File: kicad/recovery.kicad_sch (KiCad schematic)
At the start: 40 parts, among them J1 Bus_PCI_Express_x1, J4 Conn_01x02, J6 USB_C_Receptacle_USB2.0_16P, U2 RP2040, U4 W25Q128JVP, U9 MCP25625T-E/ML, X1 ABM8-272-T3, Y2 X322516MLB4SI

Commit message: update libraries
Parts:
- removed U9: MCP25625T-E/ML, MCP25625T_E_ML:QFN28_6X6MC_MCH, symbol MCP25625:MCP25625T-E_ML
- removed X1: ABM8-272-T3, ABM8-272-T3:ABM8-272-T3_ABR, symbol crystal:ABM8-272-T3
- removed Y2: X322516MLB4SI, X322516MLB4SI:OSC_X322516MLB4SI, symbol X322516MLB4SI:X322516MLB4SI
- added U1: MCP25625T-E/ML, 4in-kicad-library:QFN28_6X6MC_MCH, symbol 4in-kicad-library:MCP25625T-E_ML
- added X2: RP2040 Crystal, 4in-kicad-library:ABM8-272-T3_ABR, symbol 4in-kicad-library:ABM8-272-T3
- added Y1: X322516MLB4SI, 4in-kicad-library:X322516MLB4SI, symbol 4in-kicad-library:X322516MLB4SI
- C10, C11: LCSC PN (none) -> C1548
- C206, C207, C209, C211, C212, C213, C214, C215, C216, C40, C90, C92, C93: LCSC PN (none) -> C307331
- C208, C210: LCSC PN (none) -> C52923
- C94, C95: LCSC PN (none) -> C1555
- D1, D2: LCSC PN (none) -> C2286
- J1, J4: LCSC PN (none) -> n/a
- J6: LCSC PN (none) -> C2765186
- R1, R2: value 150 -> 1k; JLC Link https://jlcpcb.com/partdetail/23535-0603WAF1500T5E/C22808 -> https://jlcpcb.com/partdetail/12256-0402WGF1001TCE/C11702; LCSC PN (none) -> C11702; LCSC Part # C22808 -> C11702; price C$0.0013 -> C$0.0007
- R12, R30: LCSC PN (none) -> C11702
- R203, R204: LCSC PN (none) -> C25100
- R3, R4: LCSC PN (none) -> C25905
- R91: LCSC PN (none) -> C25744
- S1, S2: LCSC PN (none) -> C318884
- U2: LCSC C2040 -> (none); LCSC PN (none) -> C2040
- U4: footprint Package_SON:WSON-8-1EP_6x5mm_P1.27mm_EP3.4x4.3mm -> Package_SON:Fairchild_MicroPak-6_1.0x1.45mm_P0.5mm; LCSC C190862 -> (none); LCSC PN (none) -> C190862
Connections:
- net +3.3V: now also U1.11 (VIO), U1.3 (VDD)
- net +5V: now also U1.19 (VDDA)
- net CANINT: now also U1.25 (*INT)
- net CANN: now also U1.12 (CANL)
- net CANP: now also U1.13 (CANH)
- net CANRESET: now also U1.2 (*RESET)
- net CANSTBY: now also U1.15 (STBY)
- net CS: now also U1.1 (*CS)
- net GND: now also U1.18 (VSS), U1.22 (GND), U1.29 (EPAD), X2.2, X2.4, Y1.2, Y1.4
- net OSC1: now also U1.21 (OSC1), Y1.1
- net OSC2: now also U1.20 (OSC2), Y1.3
- net SCK: now also U1.26 (SCK)
- net SI: now also U1.27 (SI)
- net SO: now also U1.28 (SO)
- net XIN: now also X2.1
- net XOUT_pre: now also X2.3
- net rx: now also U1.10 (RXD), U1.5 (RXCAN)
- net tx: now also U1.16 (TXD), U1.4 (TXCAN)

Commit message: add wago connectors, update components with chips from new library
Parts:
- removed J4: Conn_01x02, Connector_PinHeader_2.54mm:PinHeader_1x02_P2.54mm_Vertical, symbol Connector_Generic:Conn_01x02
- removed S1, S2: TS-1187A-B-A-B, TS-1187A-B-A-B:SW_TS-1187A-B-A-B, symbol TS-1187A-B-A-B:TS-1187A-B-A-B
- added J2, J3: wago 2060-452/998-404, recovery:wago-2060-452_998-404, symbol recovery:wago-2060-452_998-404
- added J4: Conn_01x04, Connector:NS-Tech_Grove_1x04_P2mm_Vertical, symbol Connector_Generic:Conn_01x04
- added S1, S2: TS-1187A-B-A-B, 4in-kicad-library:TS-1187A-B-A-B, symbol 4in-kicad-library:TS-1187A-B-A-B
- U4: footprint Package_SON:Fairchild_MicroPak-6_1.0x1.45mm_P0.5mm -> Package_SON:WSON-8-1EP_6x5mm_P1.27mm_EP3.4x4.3mm
- renumbered U1 to U9, X2 to X1, Y1 to Y2
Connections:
- net +3.3V: now also J4.3 (Pin_3)
- net GND: now also J4.4 (Pin_4), S1.A, S1.B, S2.A, S2.B
- net RUN: now also S2.C, S2.D
- net SWCLK: now also J4.1 (Pin_1)
- net SWD: now also J4.2 (Pin_2)
- net ~{USB_BOOT_S}: now also S1.C, S1.D
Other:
- moved on the sheet: D2, R2

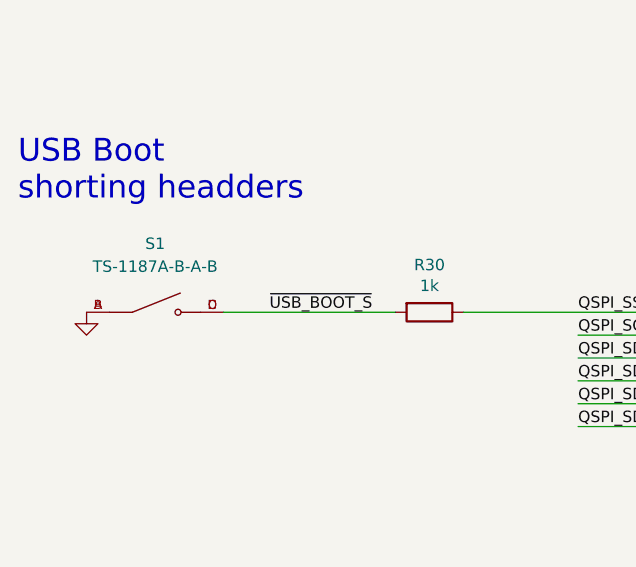
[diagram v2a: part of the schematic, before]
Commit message: rename symbol and footprint editor
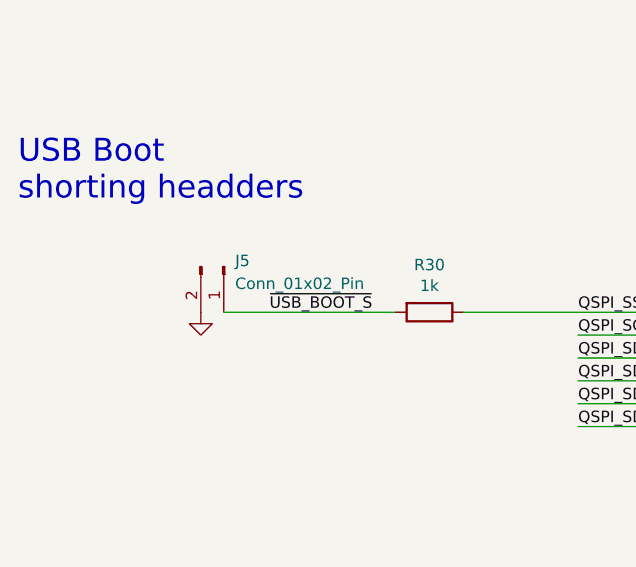
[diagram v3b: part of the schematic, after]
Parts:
- removed S1: TS-1187A-B-A-B, 4in-kicad-library:TS-1187A-B-A-B, symbol 4in-kicad-library:TS-1187A-B-A-B
- added J5: Conn_01x02_Pin, Connector_PinHeader_2.54mm:PinHeader_1x02_P2.54mm_Vertical, symbol Connector:Conn_01x02_Pin
- J4: footprint Connector:NS-Tech_Grove_1x04_P2mm_Vertical -> Connector_PinHeader_2.54mm:PinHeader_1x04_P2.54mm_Vertical
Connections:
- net GND: now also J5.2 (Pin_2)
- net ~{USB_BOOT_S}: now also J5.1 (Pin_1)
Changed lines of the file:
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@@
 	)
 	(symbol
+		(lib_id "Connector:Conn_01x02_Pin")
+		(at 69.85 162.56 270)
+		(unit 1)
+		(exclude_from_sim no)
+		(in_bom yes)
+		(on_board yes)
+		(dnp no)
+		(fields_autoplaced yes)
+		(property "Reference" "J5"
+			(at 71.12 161.9249 90)
+			(effects
+				(font
+					(size 1.27 1.27)
+				)
+				(justify left)
+			)
+		)
+		(property "Value" "Conn_01x02_Pin"
+			(at 71.12 164.4649 90)
+			(effects
+				(font
+					(size 1.27 1.27)
+				)
+				(justify left)
+			)
+		)
+		(property "Footprint" "Connector_PinHeader_2.54mm:PinHeader_1x02_P2.54mm_Vertical"
+			(at 69.85 162.56 0)
+			(effects
+				(font
+					(size 1.27 1.27)
+				)
+				(hide yes)
+			)
+		)
+		(property "Datasheet" "~"
+			(at 69.85 162.56 0)
+			(effects
+				(font
+					(size 1.27 1.27)
+				)
+				(hide yes)
+			)
+		)
+		(property "Description" "Generic connector, single row, 01x02, script generated"
+			(at 69.85 162.56 0)
+			(effects
+				(font
+					(size 1.27 1.27)
+				)
+				(hide yes)
+			)
+		)
+		(pin "1"
+		)
+		(pin "2"
+		)
+		(instances
+			(project ""
+				(path "/612ece3f-e722-4b33-8111-645d24cfcf05"
+					(reference "J5")
+					(unit 1)
+				)
+			)
+		)
+	)
+	(symbol
 		(lib_id "power:GND")
 		(at 274.32 219.71 0)
@@
 	(symbol
 		(lib_id "power:GND")
-		(at 54.61 167.64 0)
+		(at 67.31 167.64 0)
 		(unit 1)
 		(exclude_from_sim no)
@@
 		(dnp no)
 		(property "Reference" "#PWR011"
-			(at 54.61 173.99 0)
+			(at 67.31 173.99 0)
 			(effects
 				(font
@@
 		)
 		(property "Value" "GND"
-			(at 54.737 172.0342 0)
+			(at 67.437 172.0342 0)
 			(effects
 				(font
@@
 		)
 		(property "Footprint" ""
-			(at 54.61 167.64 0)
+			(at 67.31 167.64 0)
 			(effects
 				(font
@@
 		)
 		(property "Datasheet" ""
-			(at 54.61 167.64 0)
+			(at 67.31 167.64 0)
 			(effects
 				(font
@@
 		)
 		(property "Description" ""
-			(at 54.61 167.64 0)
+			(at 67.31 167.64 0)
 			(effects
 				(font
@@
 			)
 		)
-		(property "Footprint" "Connector:NS-Tech_Grove_1x04_P2mm_Vertical"
+		(property "Footprint" "Connector_PinHeader_2.54mm:PinHeader_1x04_P2.54mm_Vertical"
 			(at 243.84 212.09 0)
 			(effects
@@
 					(unit 1)
 				)
-			)
-		)
-	)
-	(symbol
-		(lib_id "4in-kicad-library:TS-1187A-B-A-B")
-		(at 62.23 167.64 0)
-		(unit 1)
-		(exclude_from_sim no)
-		(in_bom yes)
-		(on_board yes)
-		(dnp no)
-		(fields_autoplaced yes)
-		(property "Reference" "S1"
-			(at 62.23 160.02 0)
-			(effects
-				(font
-					(size 1.27 1.27)
-				)
-			)
-		)
-		(property "Value" "TS-1187A-B-A-B"
-			(at 62.23 162.56 0)
-			(effects
-				(font
-					(size 1.27 1.27)
-				)
-			)
-		)
-		(property "Footprint" "4in-kicad-library:TS-1187A-B-A-B"
-			(at 62.23 167.64 0)
-			(effects
-				(font
-					(size 1.27 1.27)
-				)
-				(justify bottom)
-				(hide yes)
-			)
-		)
-		(property "Datasheet" "https://jlcpcb.com/api/file/downloadByFileSystemAccessId/8550724022091735041"
-			(at 62.23 167.64 0)
-			(effects
-				(font
-					(size 1.27 1.27)
-				)
-				(hide yes)
-			)
-		)
-		(property "Description" "Button"
-			(at 62.23 167.64 0)
-			(effects
-				(font
-					(size 1.27 1.27)
-				)
-				(hide yes)
-			)
-		)
-		(property "JLC Link" "https://jlcpcb.com/partdetail/XKBConnection-TS_1187A_B_AB/C318884"
-			(at 62.23 167.64 0)
-			(effects
-				(font
-					(size 1.27 1.27)
-				)
-				(hide yes)
-			)
-		)
-		(property "LCSC PN" "C318884"
-			(at 62.23 167.64 0)
-			(effects
-				(font
-					(size 1.27 1.27)
-				)
-				(hide yes)
-			)
-		)
-		(property "JLC Price" "0.0242 "
-			(at 62.23 167.64 0)
-			(effects
-				(font
-					(size 1.27 1.27)
-				)
-				(hide yes)
-			)
-		)
-		(property "Manufacturer PN" "TS-1187A-B-A-B"
-			(at 62.23 167.64 0)
-			(effects
-				(font
-					(size 1.27 1.27)
-				)
-				(hide yes)
-			)
-		)
-		(pin "C"
-		)
-		(pin "D"
-		)
-		(pin "A"
-		)
-		(pin "B"
-		)
-		(instances
-			(project ""
-				(path "/612ece3f-e722-4b33-8111-645d24cfcf05"
-					(reference "S1")
-					(unit 1)
-				)

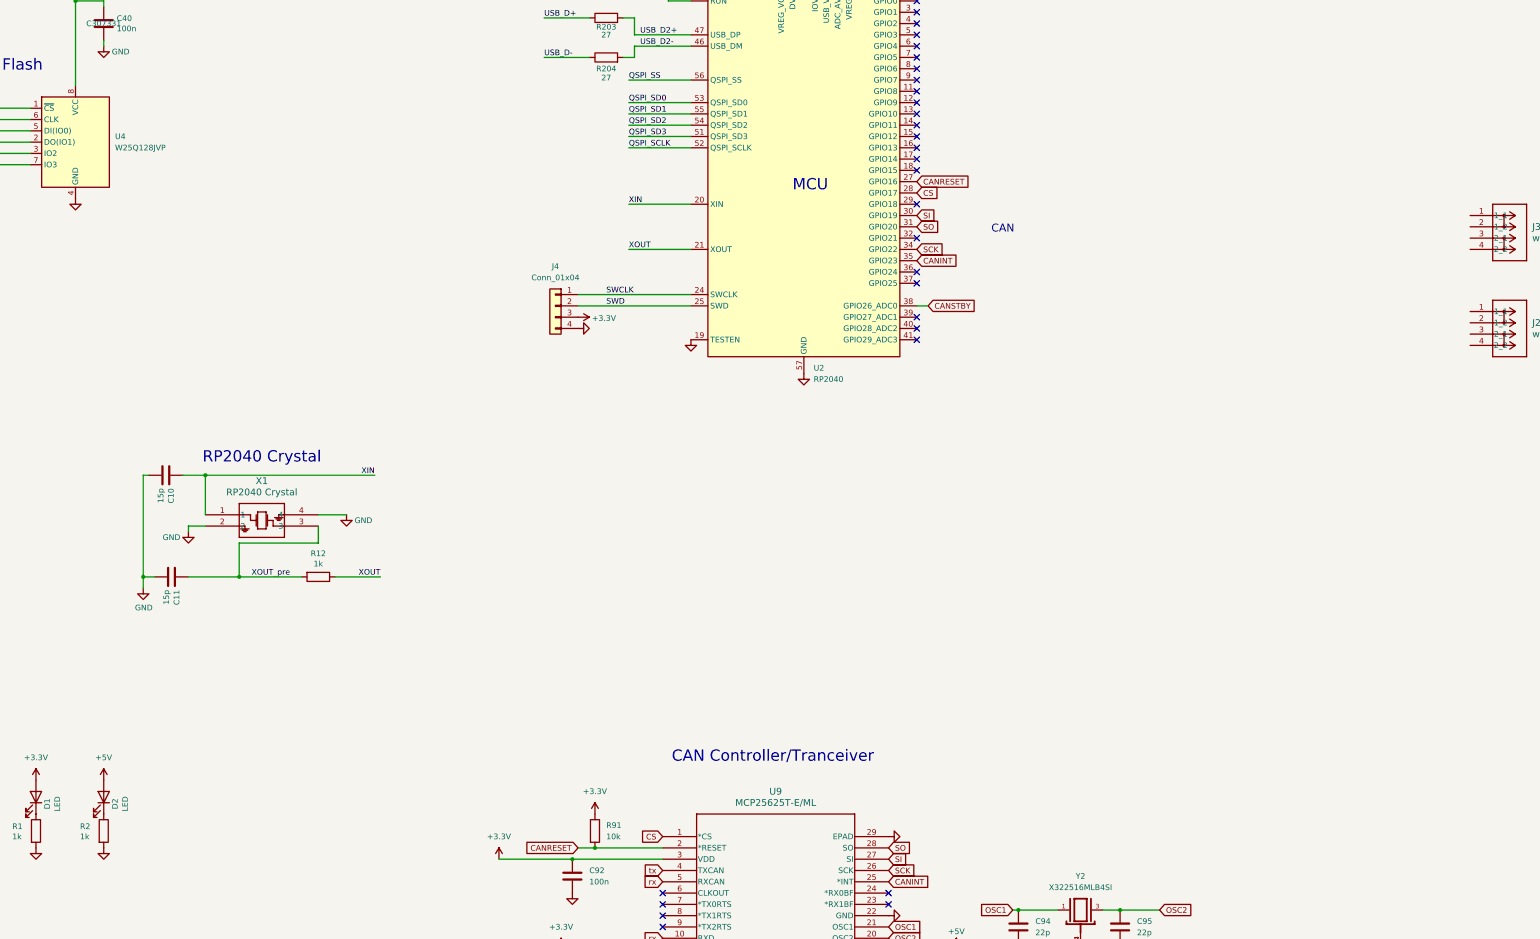
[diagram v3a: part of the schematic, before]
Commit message: add dual N channel mosfet symbol and footprint
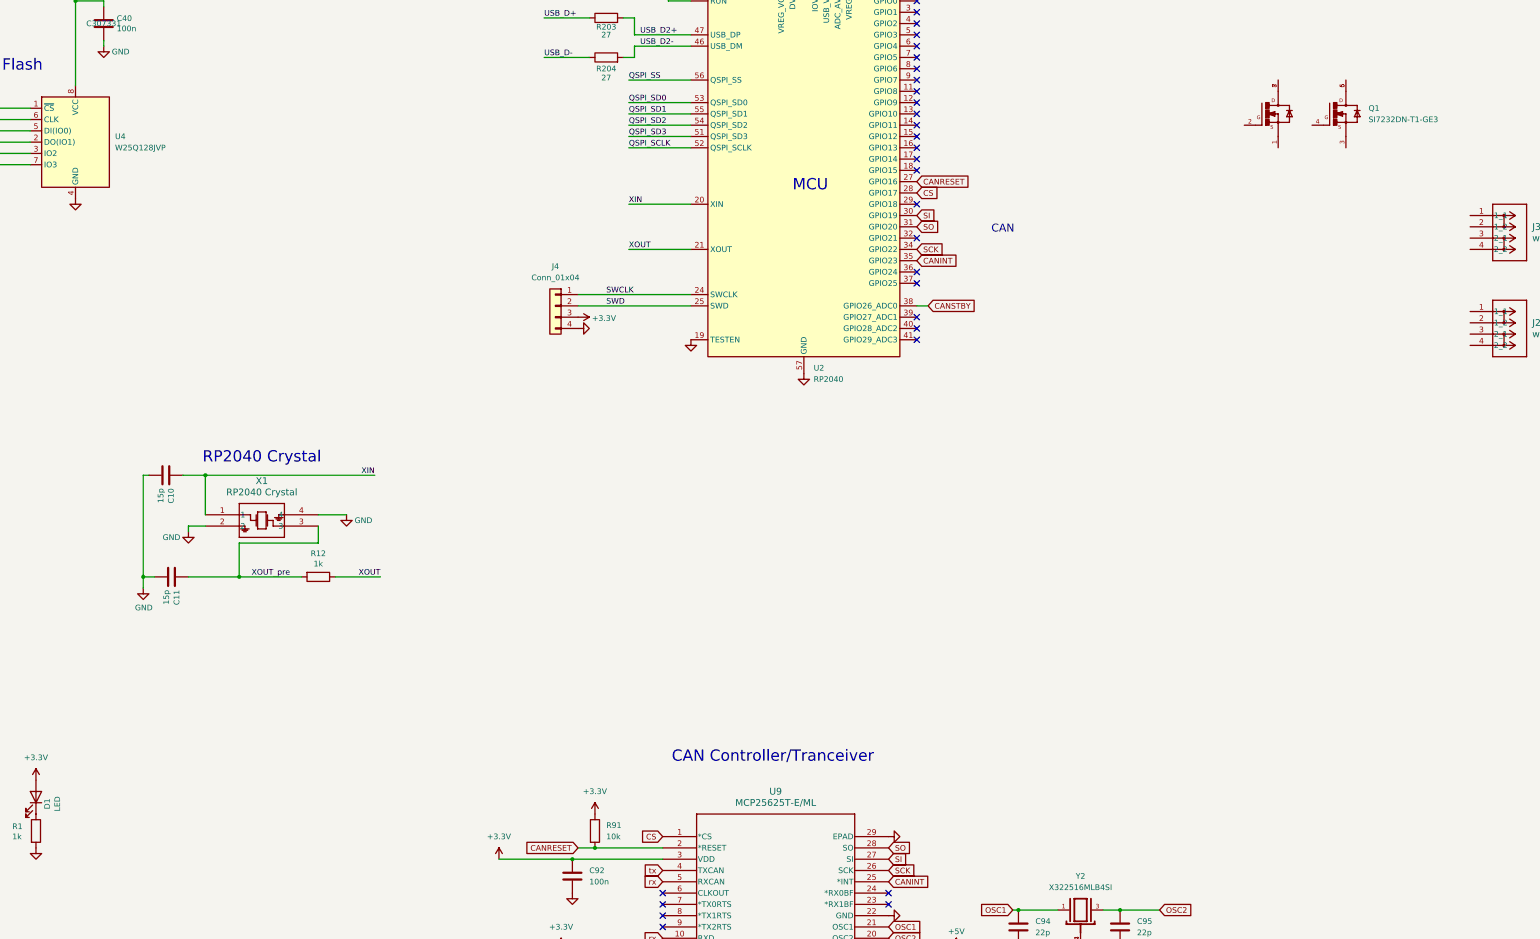
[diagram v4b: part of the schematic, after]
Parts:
- removed D2: LED, LED_SMD:LED_0603_1608Metric, symbol Device:LED
- removed R2: 1k, Resistor_SMD:R_0603_1608Metric, symbol Device:R
- added Q1: SI7232DN-T1-GE3, 4in-recovery:SI7232DN-T1-GE3, symbol 4in-recovery:SI7232DN-T1-GE3
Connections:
- new net: Q1.5, Q1.6
- new net: Q1.7, Q1.8

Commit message: add proper net names to recovery section
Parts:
- added R10, R8: 100k, Resistor_SMD:R_0402_1005Metric, symbol Device:R
- added R11, R9: 27k, Resistor_SMD:R_0402_1005Metric, symbol Device:R
- added R2, R7: 100, Resistor_SMD:R_0402_1005Metric, symbol Device:R
- added R5, R6: 3.3k, Resistor_SMD:R_0402_1005Metric, symbol Device:R
- J2, J3: footprint recovery:wago-2060-452_998-404 -> 4in-recovery:wago-2060-452_998-404
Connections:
- net GND: now also Q1.1, Q1.3, R11.1, R5.1, R6.1, R9.1
- net v_lipo: now reaches J1.A16 (PERp0)
- net v_lipo: now also J1.A17 (PERn0), J1.A18 (GND), J1.B16 (GND), J1.B17 (~{PRSNT2}), J1.B18 (GND), J2.3 (2_1), J2.4 (2_2), J3.3 (2_1), J3.4 (2_2)
- net at Q1.2: now also R7.2
- net at Q1.4: now also R2.2
- net at Q1.5, Q1.6: now also J3.1 (1_1), J3.2 (1_2), R8.2
- net at Q1.7, Q1.8: now also J2.1 (1_1), J2.2 (1_2), R10.2
- new net fire_d: R2.1, R5.2
- new net fire_m: R6.2, R7.1
- new net sense_d: R8.1, R9.2
- new net sense_m: R10.1, R11.2
- no-connect marks 43 -> 37
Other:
- moved on the sheet: J2, J3, Q1

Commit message: begin fet routing
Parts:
- renumbered R2 to R20, R5 to R21, R8 to R22, R9 to R23, R7 to R300, R6 to R31, R10 to R32, R11 to R33
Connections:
- net fire_d: now also U2.3 (GPIO1)
- net fire_m: now also U2.2 (GPIO0)
- net sense_d: now also U2.4 (GPIO2)
- net sense_m: now also U2.5 (GPIO3)
- no-connect marks 37 -> 33

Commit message: fix outline
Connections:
- net +3.3V: now also R1.1; no longer D1.2 (A)
- net GND: now also D1.1 (K); no longer R1.2
- net fire_d: now also U2.5 (GPIO3); no longer U2.3 (GPIO1)
- net fire_m: now also U2.6 (GPIO4); no longer U2.2 (GPIO0)
- net sense_m: now also U2.7 (GPIO5); no longer U2.5 (GPIO3)
- new net: D1.2 (A), R1.2
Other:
- note added: "Parachute Circuit"
- moved on the sheet: D1, J2, R1

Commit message: update PCIe footprint
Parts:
- removed J1: Bus_PCI_Express_x1, Connector_PCBEdge:BUS_PCIexpress_x1, symbol Connector:Bus_PCI_Express_x1
- removed R1: 1k, Resistor_SMD:R_0603_1608Metric, symbol Device:R
- added C1: 100u, Capacitor_SMD:C_1210_3225Metric, symbol Device:C
- added J1: Bus_PCI_Express_x1, Connector_PCBEdge:BUS_PCIexpress_x1, symbol 4in-kicad-library:PCIex1
- added R2: 1k, Resistor_SMD:R_0402_1005Metric, symbol Device:R
- C10, C11: LCSC Part # C1548 -> (none)
- C206, C207, C209, C211, C212, C213, C214, C215, C216, C40, C90, C92, C93: LCSC Part # C307331 -> (none)
- C208, C210: LCSC Part # C52923 -> (none)
- C94, C95: LCSC Part # C1555 -> (none)
- D1: LCSC Part # C2286 -> (none)
- J2, J3: price (none) -> C$0.3120
- J4, J5: now not fitted
- J6: LCSC Part # C2765186 -> (none)
- Q1: price (none) -> C$0.9814
- R12, R30: LCSC Part # C11702 -> (none)
- R20, R300: JLC Link (none) -> https://jlcpcb.com/partdetail/25819-0402WGF1000TCE/C25076; LCSC PN (none) -> C25076; price (none) -> C$0.0007
- R203, R204: LCSC Part # C25100 -> (none)
- R21, R31: JLC Link (none) -> https://jlcpcb.com/partdetail/26633-0402WGF3301TCE/C25890; LCSC PN (none) -> C25890; price (none) -> C$0.0007
- R22, R32: JLC Link (none) -> https://jlcpcb.com/partdetail/26484-0402WGF1003TCE/C25741; LCSC PN (none) -> C25741; price (none) -> C$0.0007
- R23, R33: JLC Link (none) -> https://jlcpcb.com/partdetail/26294-0402WGJ0273TCE/C25551; LCSC PN (none) -> C25551; price (none) -> C$0.0003
- R3, R4: LCSC Part # C25905 -> (none)
- R91: LCSC Part # C25744 -> (none)
- S2: price (none) -> C$0.0263
- U2: LCSC Part # C2040 -> (none)
- U4: LCSC Part # C190862 -> (none)
- U9: price (none) -> C$2.1278
- X1: price (none) -> C$0.5074
- Y2: price (none) -> C$0.0742
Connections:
- net +3.3V: now also J1.A10 (+3.3V), J1.A11 (+3.3V), J1.A9 (+3.3V), J1.B10 (+3.3V), J1.B11 (+3.3V), J1.B9 (+3.3V), R2.1
- net +5V: now also J1.A12 (+5V), J1.A13 (+5V), J1.A14 (+5V), J1.B12 (+5V), J1.B13 (+5V), J1.B14 (+5V)
- net GND: now also C1.2, J1.A4 (GND), J1.A5 (GND), J1.A6 (GND), J1.A7 (GND), J1.B1 (GND), J1.B2 (GND), J1.B3 (GND), J1.B4 (GND), J1.B5 (GND), J1.B6 (GND), J1.B7 (GND)
- net sense_d: now also U2.39 (GPIO27_ADC1); no longer U2.4 (GPIO2)
- net sense_m: now also U2.40 (GPIO28_ADC2); no longer U2.7 (GPIO5)
- net v_lipo: now also C1.1, J1.A16 (VBAT), J1.A17 (VBAT), J1.A18 (VBAT), J1.B16 (VBAT), J1.B17 (VBAT), J1.B18 (VBAT)
- net at D1.2 (A): now also R2.2
- net +1.1V renamed +1V1
- net CANN renamed CANL
- net CANL: now also J1.A3 (CANN)
- net CANP renamed CANH
- net CANH: now also J1.A1 (CANH)
- no-connect marks 33 -> 34
